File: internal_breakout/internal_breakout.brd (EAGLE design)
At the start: 50 x 35 mm, 21 parts, among them J10 2X5, J11 2X5, J3 2X5, J4 2X5, Q1 DMP3099L, U1 LP2985

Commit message: push updated files for internal breakout
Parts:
- added FB1: BLM18KG700TN1D, SamacSys_Parts:BEADC1608X75N
- added J14, J15, J16: (no value), con-lstb:MA03-1
- C1: value 1uF -> 10uF
- moved C1 11.1 mm to (19.0, 13.0), turned to 0 degrees
- moved C4 10.4 mm to (15.9, 16.0), turned to 180 degrees
- moved C2 9.33 mm to (23.9, 19.0)
- moved U1 7.54 mm to (15.9, 19.0), turned to 270 degrees
- moved J2 5.83 mm to (21.9, 27.2)
- moved J1 5.83 mm to (21.9, 31.0)
- moved J13 5.41 mm to (43.9, 16.0)
- moved C3 4.74 mm to (21.9, 19.0)
- moved J5 4.54 mm to (31.4, 27.2)
- moved J6 4.53 mm to (31.4, 31.0)
- moved Q1 3.25 mm to (22.9, 10.9)
- moved J12 2.91 mm to (39.4, 16.0)
- moved C5 2.06 mm to (20.4, 16.5), turned to 0 degrees
- moved J9 1.27 mm to (40.7, 23.0)
- moved J7 0.95 mm to (40.7, 27.2)
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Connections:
- removed net NC: J4.2
- new net +10VA: C2.1, C3.1, C5.1, C6.1, J12.3, J14.3, U1.5
- new net VIN: J11.7, J11.8, Q1.3
- net CH10: now also J4.6; no longer J4.8
- net CH11: now also J4.3; no longer J4.5
- net CH12: now also J4.4; no longer J4.6
- net CH13: now also J4.1; no longer J4.3
- net CH14: now also J4.2; no longer J4.4
- net CH15: no longer J4.1
- net CH7: now also J15.3, J4.7
- net CH8: now also J16.3, J4.8
- net CH9: now also J4.5; no longer J4.7
- net GND: now also J15.2, J16.2
- net N$1: now also FB1.1; no longer C1.1, U1.1, U1.3
- net V+: now also J14.2, J15.1, J16.1; no longer C2.1, C3.1, C5.1, C6.1, J12.3, J13.3, U1.5
- net VCC: now also C1.1, FB1.2, J13.3, J14.1, U1.1, U1.3; no longer J11.7, J11.8, Q1.3
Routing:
- net CH12: track 62.3 -> 118.4 mm
- net CH11: track 69.3 -> 121.5 mm, vias 1 -> 3
- net CH8: track 56.9 -> 93.4 mm, vias 2 -> 0
- net VCC: track 12.3 -> 47.3 mm
- net CH9: track 63.6 -> 90.7 mm, vias 2 -> 1
- net CH7: track 54.4 -> 80.9 mm, vias 2 -> 1
- net +10VA: track 0.00 -> 25.8 mm
- net CH15: track 78.8 -> 56.4 mm, vias 1 -> 2
- net V+: track 136.2 -> 116.1 mm
- net CH10: track 65.7 -> 82.7 mm, vias 2 -> 1
- net CH13: track 80.7 -> 92.8 mm, vias 3 -> 2
- net CH2: track 51.9 -> 63.0 mm, vias 0 -> 1
- net N$1: track 11.2 -> 2.44 mm
- net VIN: track 0.00 -> 7.12 mm
- net CH4: track 50.5 -> 56.9 mm
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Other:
- board text added: "1"
- board text added: "10V"
- board text added: "2"
- board text added: "A"
- board text added: "B"
- board text added: "CH7"
- board text added: "CH8"
- board text added: "INTERNAL BREAKOUT V2.2"
- board text added: "J15"
- board text added: "J16"
- board text added: "NU MULTI INPUT"
- board text added: "PWR SELECT"
- board text added: "UNREG_VCC"
- board text added: "VCC"
- board text removed: "+10V"
- board text removed: "ANALOG INPUTS"
- board text removed: "CH1 - CH8"
- board text removed: "CH9 - CH15"
- board text removed: "Internal Breakout v2.0"
- board text removed: "J10"
- board text removed: "J11"
- board text removed: "J3"
- board text removed: "J4"
- board text removed: "LEMO OUT"
- board text removed: "SUPPLY EXTENSION"

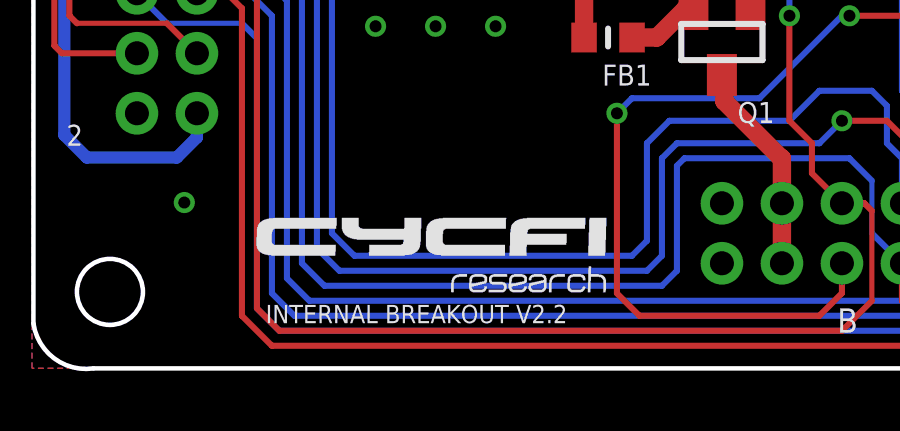
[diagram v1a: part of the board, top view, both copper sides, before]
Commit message: update internal breakout files
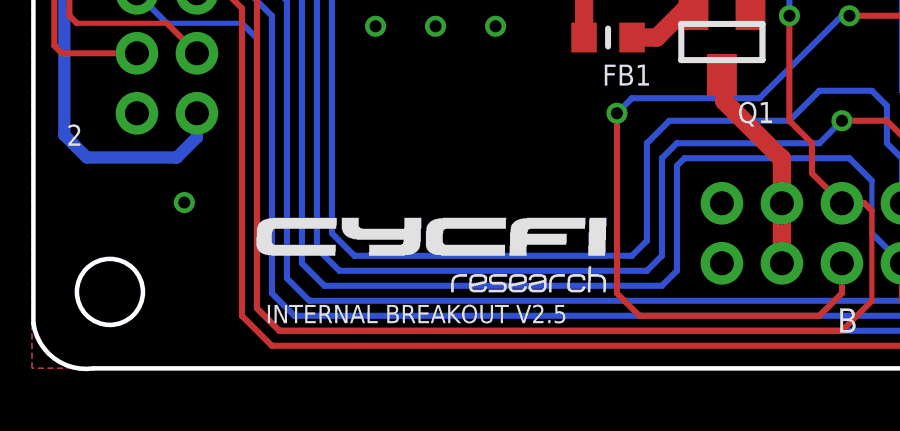
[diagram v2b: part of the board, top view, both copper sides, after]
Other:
- board text added: "INTERNAL BREAKOUT V2.5"
- board text removed: "INTERNAL BREAKOUT V2.2"
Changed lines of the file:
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@@
 <rectangle x1="16.42109375" y1="4.975859375" x2="18.3718125" y2="4.991096875" layer="25"/>
 <rectangle x1="18.508971875" y1="4.975859375" x2="19.072853125" y2="4.991096875" layer="25"/>
-<text x="7.7114375" y="1.478278125" size="0.6096" layer="25" font="vector" ratio="12">INTERNAL BREAKOUT V2.2</text>
+<text x="7.7114375" y="1.478278125" size="0.6096" layer="25" font="vector" ratio="12">INTERNAL BREAKOUT V2.5</text>
 <text x="1.239" y="14.658" size="0.8128" layer="25" font="vector" ratio="12" rot="R90">NU MULTI INPUT</text>
 <text x="38.451" y="1.995" size="0.8128" layer="25" font="vector" ratio="12" rot="R180">A</text>

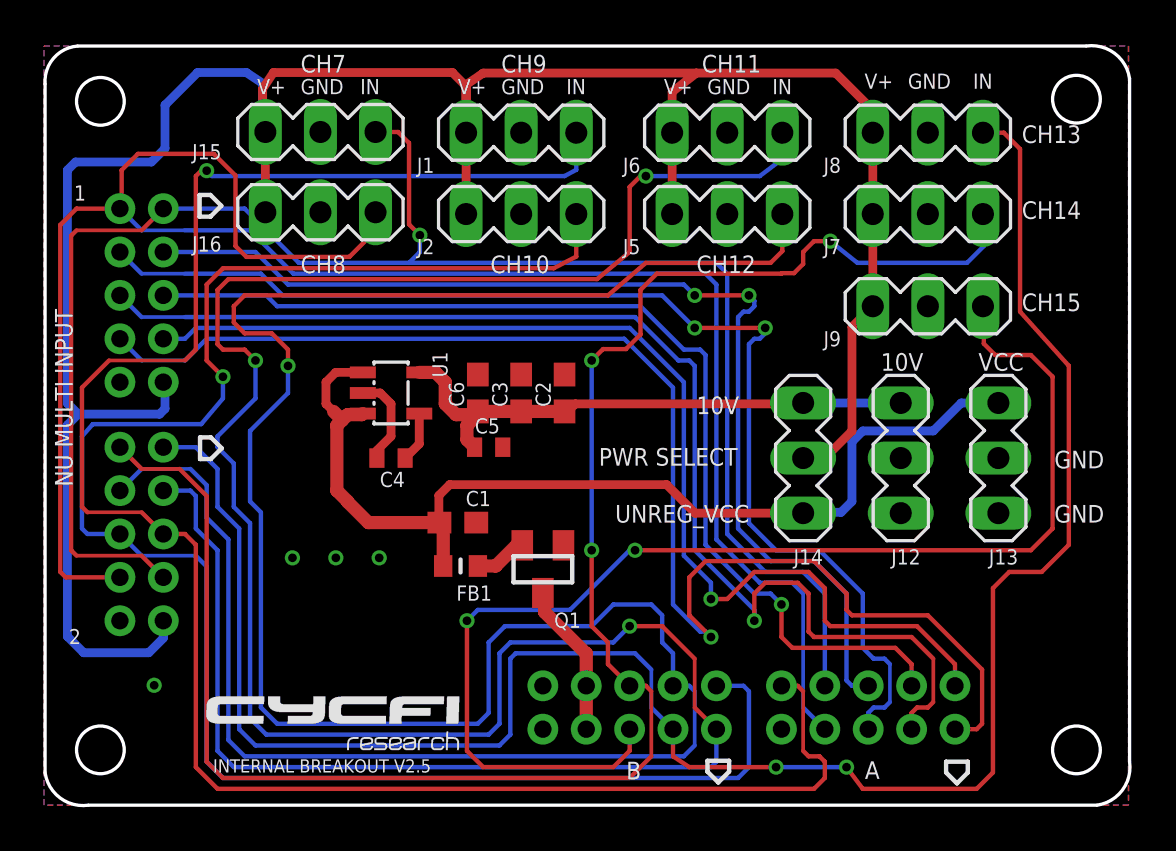
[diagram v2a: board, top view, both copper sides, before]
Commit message: update internal breakout with special header for 2 way switch
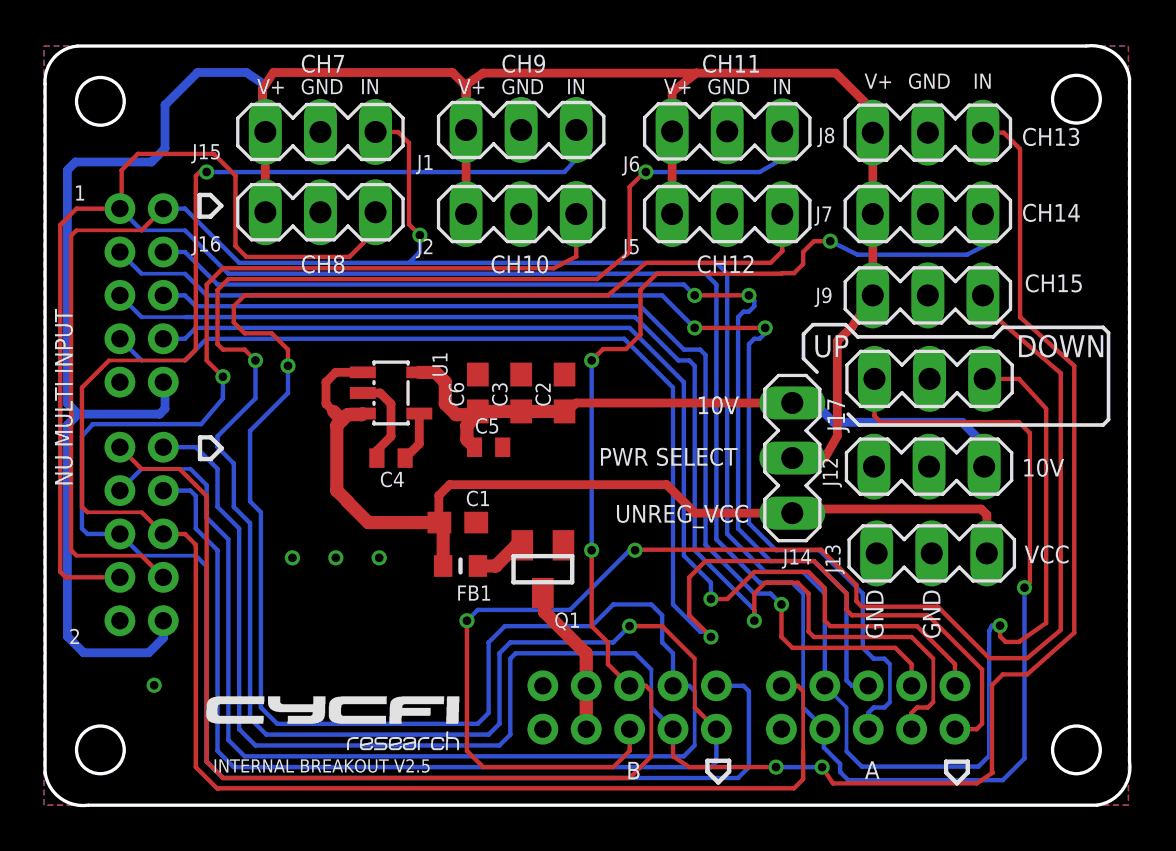
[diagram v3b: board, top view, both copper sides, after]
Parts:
- added J17: (no value), con-lstb:MA03-1
- moved J13 5.36 mm to (40.9, 11.6), turned to 0 degrees
- moved J12 1.36 mm to (40.7, 15.6), turned to 0 degrees
- moved J14 0.50 mm to (34.4, 16.0)
- moved J9 0.50 mm to (40.7, 23.5)
- moved J1 0.12 mm to (21.9, 31.1)
- moved J6 0.06 mm to (31.4, 31.0)
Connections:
- net CH7: now also J17.3
- net CH8: now also J17.1
- net GND: now also J17.2
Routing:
- net CH8: track 93.4 -> 129.0 mm, vias 0 -> 1
- net CH7: track 80.9 -> 114.1 mm, vias 1 -> 2
- net CH15: track 56.4 -> 63.9 mm
- net +10VA: track 25.8 -> 31.5 mm
- net VCC: track 47.3 -> 45.0 mm
- net CH9: track 90.7 -> 88.7 mm
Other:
- board text added: "DOWN"
- board text added: "UP"
